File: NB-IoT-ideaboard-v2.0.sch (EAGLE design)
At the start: 98 parts, among them Q1 32.768kHz, Q2 8MHz, Q3 9013, Q4 9013, Q5 9013, U1 STM32F103RBT6, U2 MCP73831T-2ACI/OT, U3 AP2112-3.3, U4 PAM2401, U5 MICROSIM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

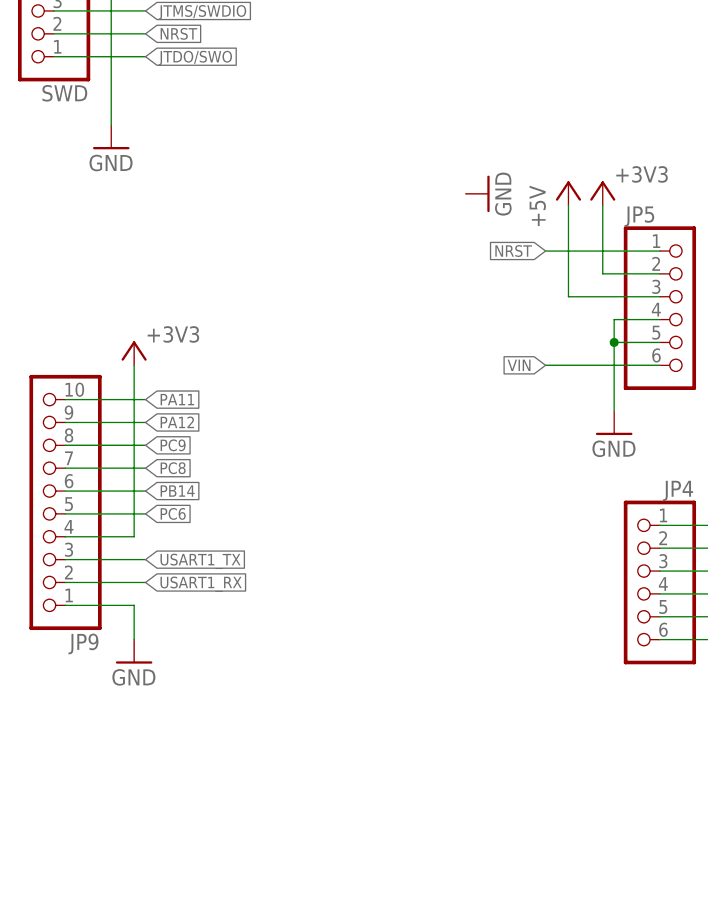
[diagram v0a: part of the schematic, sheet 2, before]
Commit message: Adds logos, mounting holes
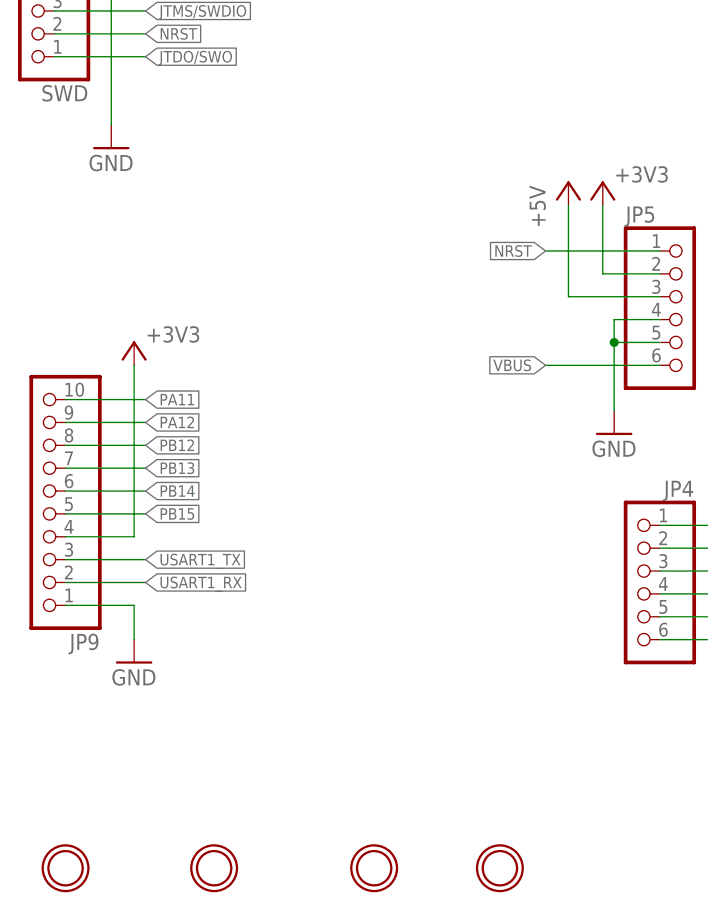
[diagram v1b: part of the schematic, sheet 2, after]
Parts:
- added $H1, $H2, $H3, $H4: MOUNTINGHOLE3.0THIN, Adafruit SIM808 Breakout:MOUNTINGHOLE3.0THIN
- renumbered CONFIG to BOOT, JP1 to MODEMCTL
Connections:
- removed net VIN: JP5.6
- net PB12: now also JP9.8
- net PB13: now also JP9.7
- net PB15: now also JP9.5
- net PC6: no longer JP9.5
- net PC8: no longer JP9.7
- net PC9: no longer JP9.8
- net VBUS: now also JP5.6

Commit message: Minor changes
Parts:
- removed $H4: MOUNTINGHOLE3.0THIN, Adafruit SIM808 Breakout:MOUNTINGHOLE3.0THIN
- R1: value 1k -> 330R
- R13, R28: value 2.2k -> 2k2
- R19, R20, R26: value 4.7k -> 4k7
- R25: value 2.2k -> 0R
- R6: value 5.6k -> 5k7
- S1: device SparkFun-Electromechanical:SWITCH-SPDTSMD2 -> SparkFun-Electromechanical:SWITCH-SPDT-SMD-A
- renumbered ANT1 to RF_ANT
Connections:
- net +3V3: now also R1.2
- net +5V: no longer R1.2
- net PA4: now also CC1101.4
- net PB6: no longer CC1101.4

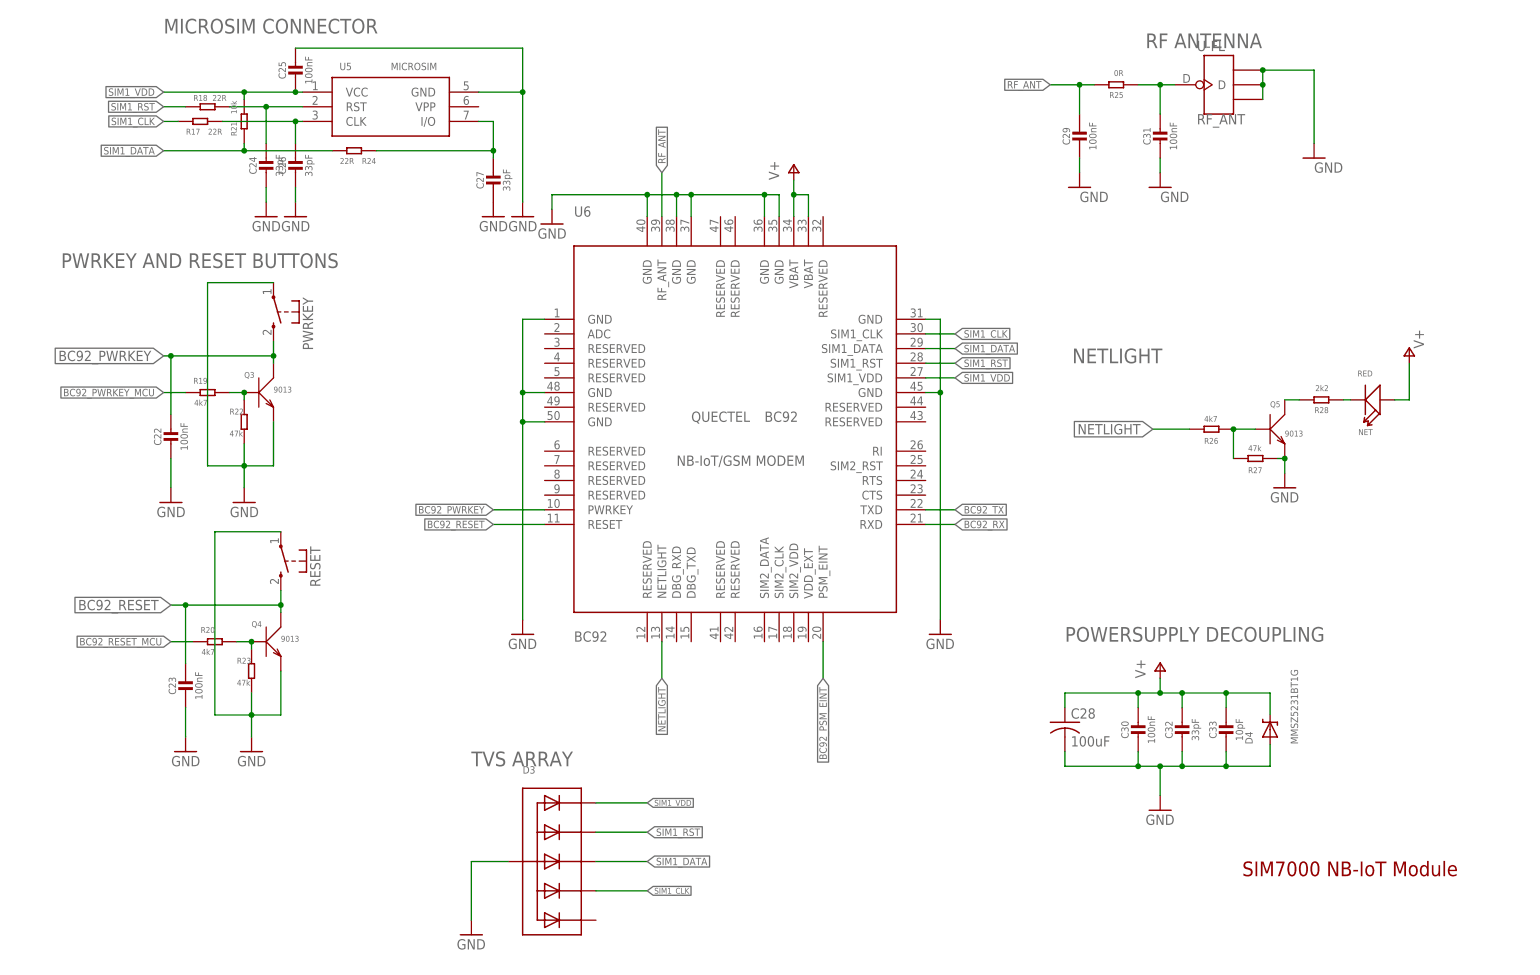
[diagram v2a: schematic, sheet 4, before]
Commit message: Adjust USB port
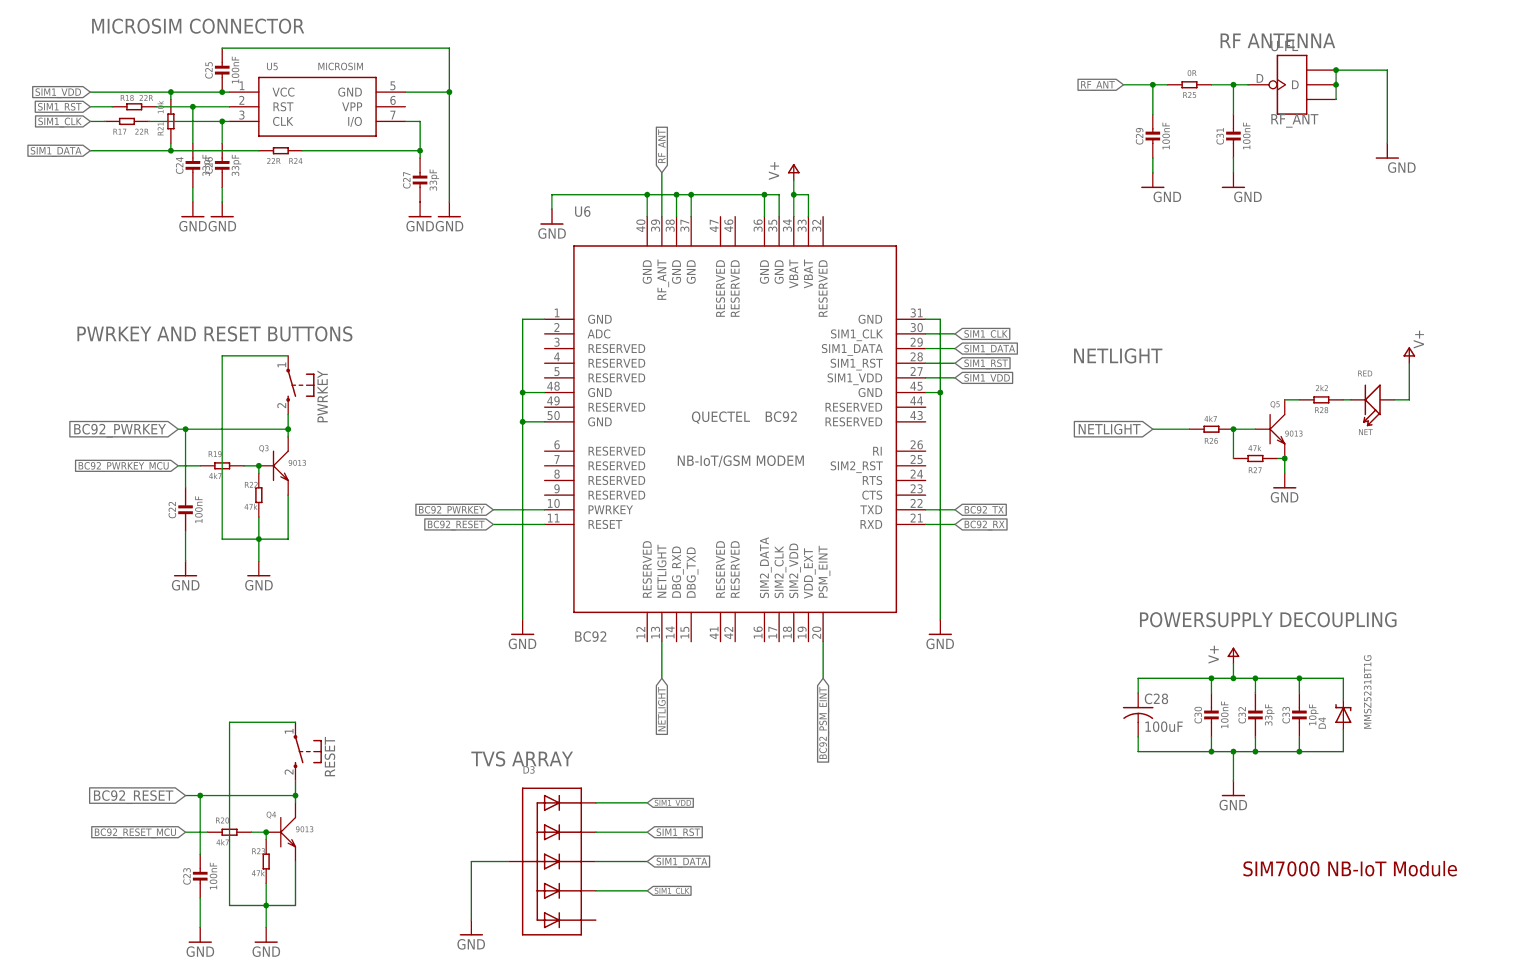
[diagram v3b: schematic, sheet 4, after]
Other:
- moved on the sheet: C22, C23, C24, C25, C26, C27, C28, C29, C30, C31, C32, C33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

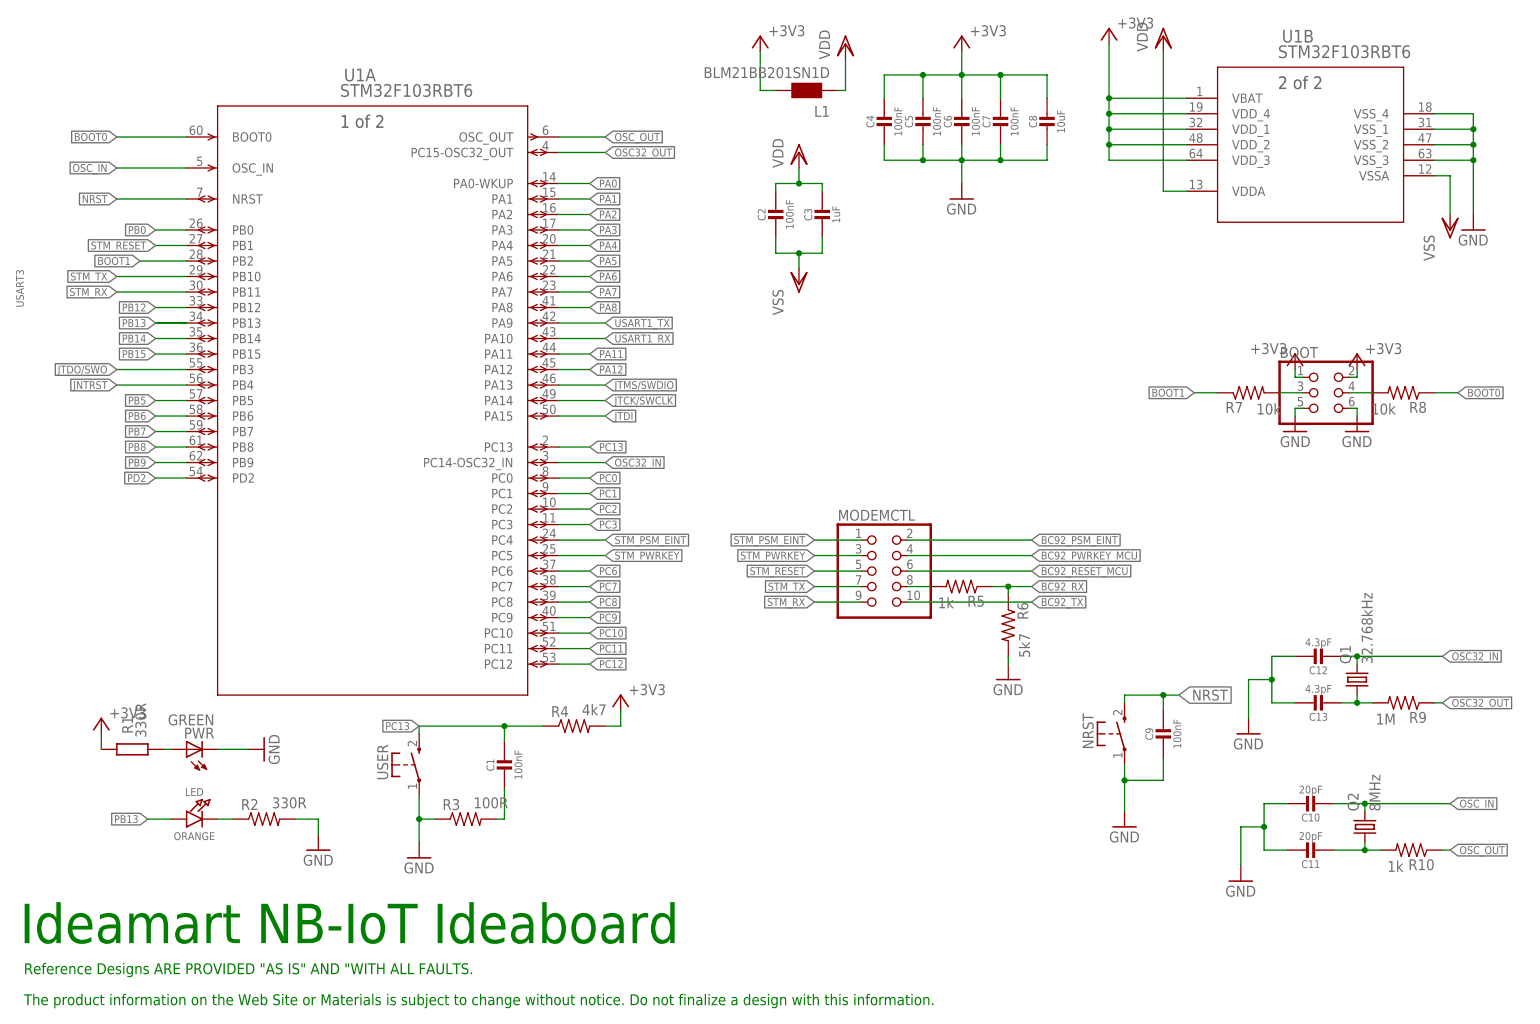
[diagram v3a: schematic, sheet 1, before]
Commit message: JLCPCB layout started
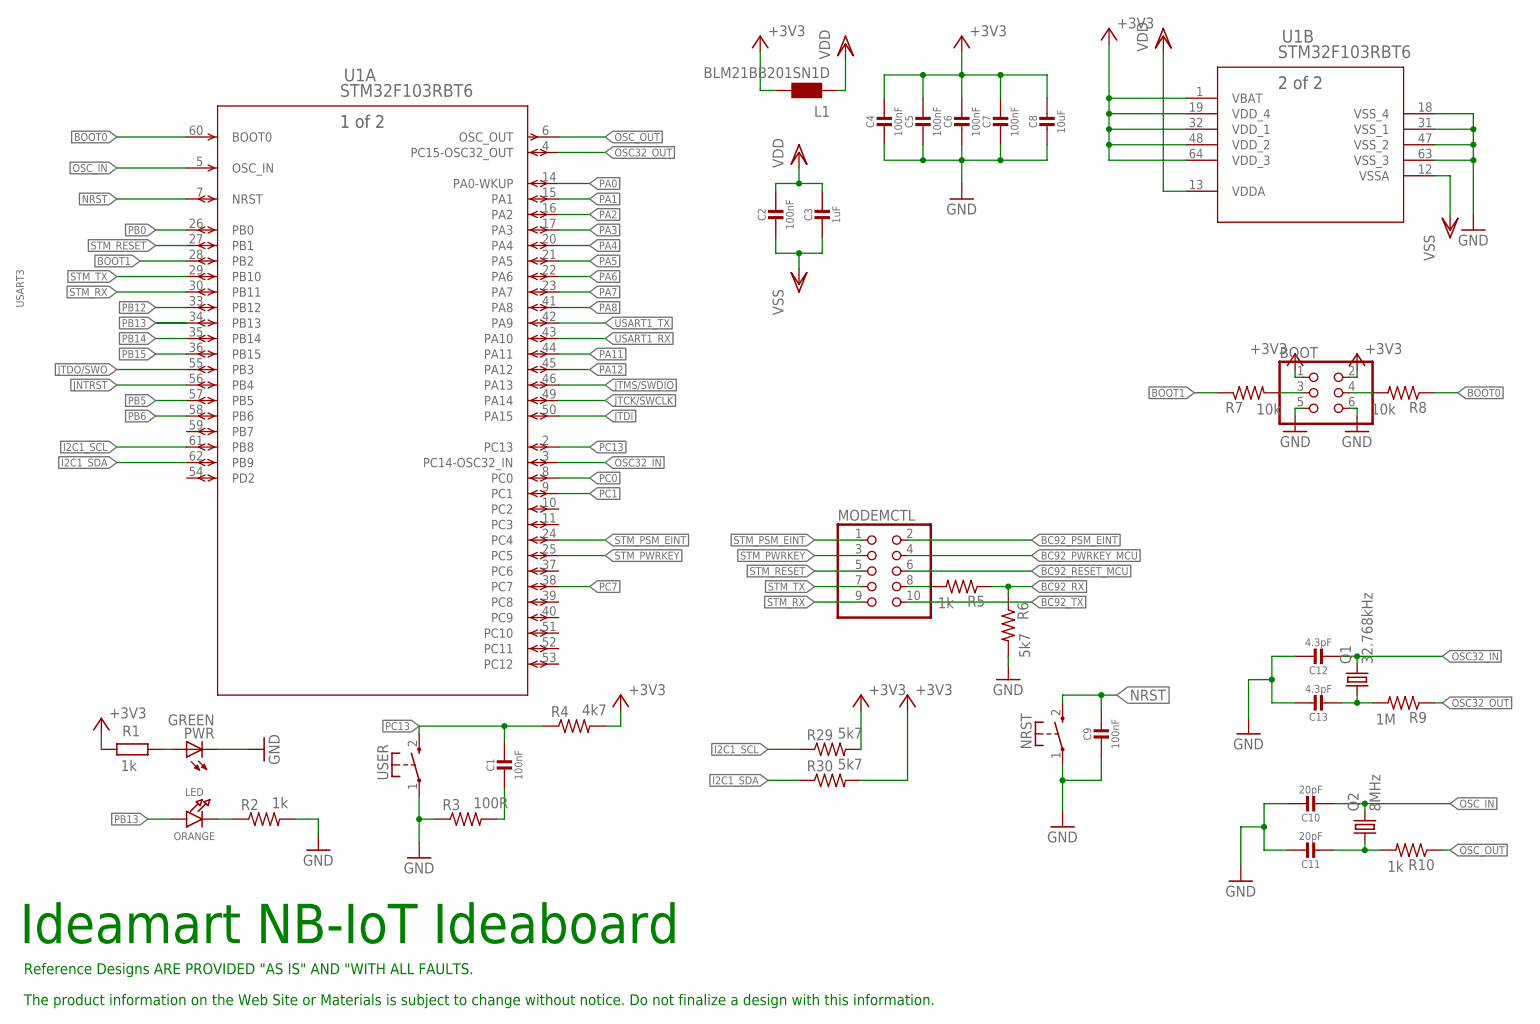
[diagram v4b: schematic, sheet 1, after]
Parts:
- added R29, R30: 5k7, resistor:R-US_M0805
- added U7: SIM-ST-MFF2, SIM-ST-MFF2:SIM-ST-MFF2
- R1, R2: value 330R -> 1k
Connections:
- removed net PB7: U1A.PB7
- removed net PB8: JP6.1, U1A.PB8
- removed net PB9: JP6.2, U1A.PB9
- removed net PC10: U1A.PC10
- removed net PC11: U1A.PC11
- removed net PC12: U1A.PC12
- removed net PC2: U1A.PC2
- removed net PC3: U1A.PC3
- removed net PC6: U1A.PC6
- removed net PC8: U1A.PC8
- removed net PC9: U1A.PC9
- removed net PD2: U1A.PD2
- new net I2C1_SCL: JP6.1, R29.1, U1A.PB8
- new net I2C1_SDA: JP6.2, R30.1, U1A.PB9
- net +3V3: now also R29.2, R30.2
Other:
- moved on the sheet: C9, NRST
